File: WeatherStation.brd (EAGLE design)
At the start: 30.5 x 53.3 mm, 36 parts, among them J1 EDISON_CONNECTOR_FULLMOUNTING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, J2 EDISON_CONNECTOR_FULLHEADER, U1 MCP73831, U2 HTU21D, U3 MPL3115A2, U4 PCA9306

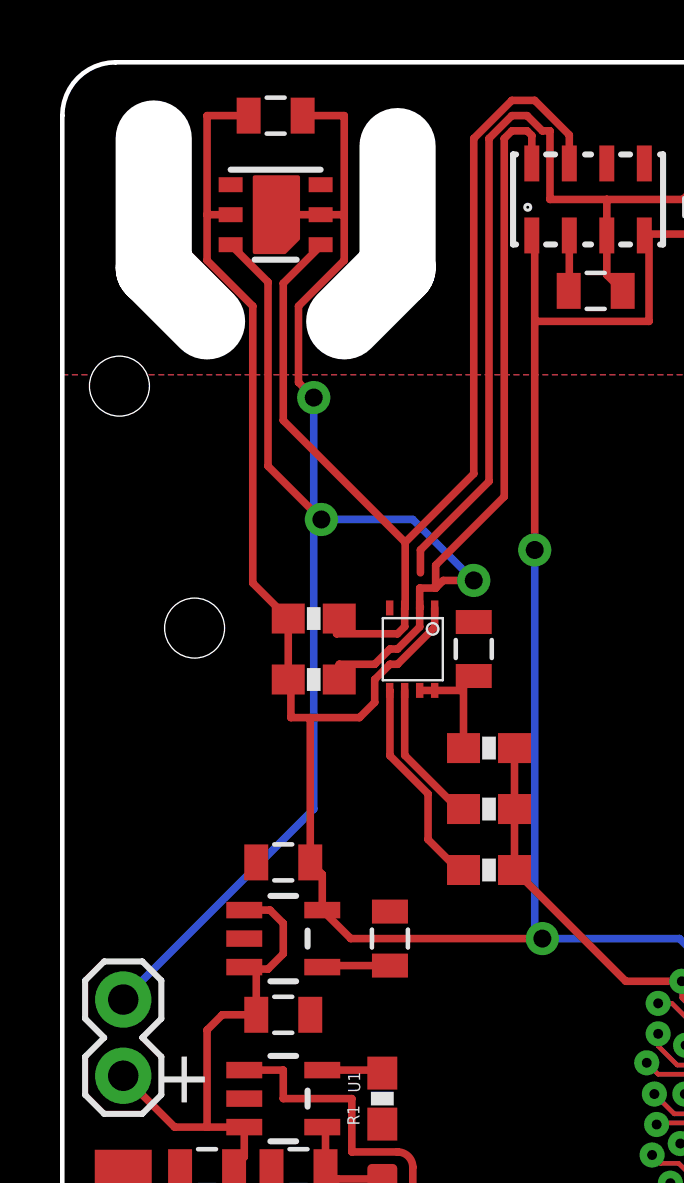
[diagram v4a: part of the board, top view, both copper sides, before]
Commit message: removed unnecessary GND trace and via
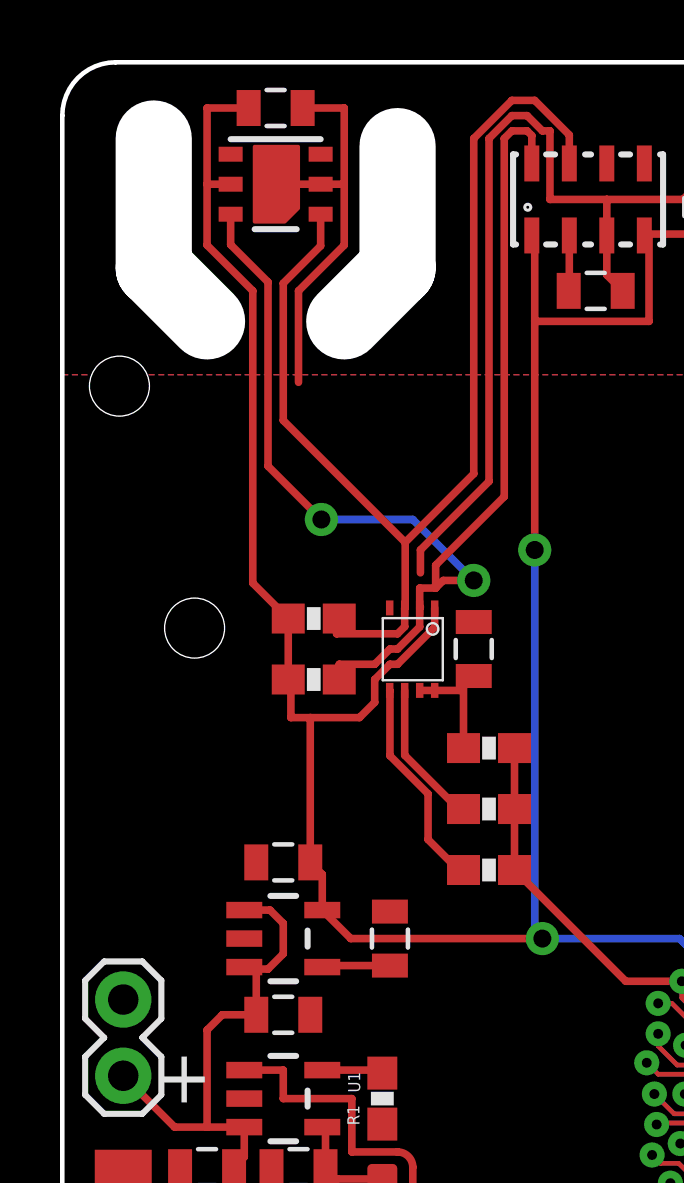
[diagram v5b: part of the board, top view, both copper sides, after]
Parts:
- moved U2 1.02 mm to (7.11, 49.3)
- moved C8 0.25 mm to (7.11, 51.8)
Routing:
- net GND: track 69.5 -> 46.4 mm, vias 3 -> 2
- net SDA: track 37.4 -> 38.4 mm
- net SCL: track 41.2 -> 42.2 mm
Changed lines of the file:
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@@
 </element>
 <element name="JP2" library="SparkFun-Connectors" package="1X02" value="M02PTH" x="2.032" y="22.098" smashed="yes" rot="R270"/>
-<element name="U2" library="SparkFun-Sensors" package="HTU21D" value="HTU21D" x="7.112" y="48.26" smashed="yes">
-<attribute name="VALUE" x="5.787" y="46.06" size="0.5" layer="27"/>
+<element name="U2" library="SparkFun-Sensors" package="HTU21D" value="HTU21D" x="7.112" y="49.276" smashed="yes">
+<attribute name="VALUE" x="5.787" y="47.076" size="0.5" layer="27"/>
 </element>
 <element name="U3" library="SparkFun-Sensors" package="LGA8" value="MPL3115A2" x="17.526" y="48.768" smashed="yes" rot="R90">
@@
 <attribute name="VALUE" x="11.684" y="26.289" size="0.4064" layer="27"/>
 </element>
-<element name="C8" library="SparkFun-Capacitors" package="0805" value="4.7µF" x="7.112" y="51.562" smashed="yes">
-<attribute name="VALUE" x="7.112" y="50.673" size="0.4064" layer="27" align="top-center"/>
+<element name="C8" library="SparkFun-Capacitors" package="0805" value="4.7µF" x="7.112" y="51.816" smashed="yes">
+<attribute name="VALUE" x="7.112" y="50.927" size="0.4064" layer="27" align="top-center"/>
 </element>
 <element name="C9" library="SparkFun-Capacitors" package="0805" value="0.1µF" x="17.78" y="45.72" smashed="yes">
@@
 <contactref element="C6" pad="2"/>
 <contactref element="C7" pad="2"/>
-<wire x1="8.012" y1="51.562" x2="9.398" y2="51.562" width="0.254" layer="1"/>
-<wire x1="9.398" y1="51.562" x2="9.398" y2="48.26" width="0.254" layer="1"/>
-<wire x1="9.398" y1="48.26" x2="9.398" y2="46.736" width="0.254" layer="1"/>
-<wire x1="9.398" y1="46.736" x2="7.874" y2="45.212" width="0.254" layer="1"/>
-<wire x1="8.612" y1="48.26" x2="9.398" y2="48.26" width="0.254" layer="1"/>
-<wire x1="8.612" y1="48.26" x2="7.112" y2="48.26" width="0.254" layer="1"/>
+<wire x1="8.612" y1="49.276" x2="7.112" y2="49.276" width="0.254" layer="1"/>
 <wire x1="18.68" y1="45.72" x2="18.151" y2="46.249" width="0.254" layer="1"/>
 <wire x1="18.151" y1="46.249" x2="18.151" y2="47.568" width="0.254" layer="1"/>
@@
 <wire x1="14.224" y1="39.37" x2="11.938" y2="37.084" width="0.254" layer="1"/>
 <wire x1="11.938" y1="37.084" x2="11.938" y2="36.322" width="0.254" layer="1"/>
-<wire x1="7.874" y1="45.212" x2="7.874" y2="42.672" width="0.254" layer="1"/>
-<wire x1="7.874" y1="42.672" x2="8.382" y2="42.164" width="0.254" layer="1"/>
-<via x="8.382" y="42.164" extent="1-16" drill="0.6" diameter="0.254"/>
-<wire x1="8.382" y1="42.164" x2="8.382" y2="28.448" width="0.254" layer="16"/>
-<wire x1="8.382" y1="28.448" x2="2.032" y2="22.098" width="0.254" layer="16"/>
 <polygon width="0.3048" layer="1">
 <vertex x="0" y="42.926"/>
@@
 <vertex x="0" y="1.778"/>
 </polygon>
+<wire x1="8.012" y1="51.816" x2="9.398" y2="51.816" width="0.254" layer="1"/>
+<wire x1="9.398" y1="51.816" x2="9.398" y2="49.276" width="0.254" layer="1"/>
+<wire x1="9.398" y1="49.276" x2="9.398" y2="47.244" width="0.254" layer="1"/>
+<wire x1="9.398" y1="47.244" x2="7.874" y2="45.72" width="0.254" layer="1"/>
+<wire x1="7.874" y1="45.72" x2="7.874" y2="42.672" width="0.254" layer="1"/>
+<wire x1="8.612" y1="49.276" x2="9.398" y2="49.276" width="0.254" layer="1"/>
+<wire x1="26.9438" y1="22.1798" x2="28.2448" y2="22.1742" width="0" layer="19" extent="1-1"/>
+<wire x1="25.96" y1="22.18" x2="26.9438" y2="22.1798" width="0" layer="19" extent="1-16"/>
+<wire x1="25.96" y1="22.1798" x2="25.96" y2="22.18" width="0" layer="19" extent="1-16"/>
+<wire x1="25.96" y1="22.98" x2="25.96" y2="22.18" width="0" layer="19" extent="16-16"/>
 <wire x1="25.96" y1="22.9798" x2="25.96" y2="22.98" width="0" layer="19" extent="1-16"/>
-<wire x1="25.96" y1="22.18" x2="25.96" y2="22.98" width="0" layer="19" extent="16-16"/>
-<wire x1="25.96" y1="22.1798" x2="25.96" y2="22.18" width="0" layer="19" extent="1-16"/>
 <wire x1="25.96" y1="21.38" x2="25.96" y2="22.18" width="0" layer="19" extent="16-16"/>
 <wire x1="25.96" y1="21.3798" x2="25.96" y2="21.38" width="0" layer="19" extent="1-16"/>
@@
 <wire x1="25.96" y1="20.18" x2="25.96" y2="20.58" width="0" layer="19" extent="16-16"/>
 <wire x1="25.96" y1="20.1798" x2="25.96" y2="20.18" width="0" layer="19" extent="1-16"/>
-<wire x1="26.9438" y1="22.1798" x2="25.96" y2="22.18" width="0" layer="19" extent="1-16"/>
 <wire x1="27.1272" y1="20.5232" x2="25.96" y2="20.58" width="0" layer="19" extent="16-16"/>
-<wire x1="28.2448" y1="22.1742" x2="26.9438" y2="22.1798" width="0" layer="19" extent="1-1"/>
-<wire x1="11.938" y1="36.322" x2="13.716" y2="34.682" width="0" layer="19" extent="1-1"/>
-<wire x1="10.914" y1="35.152" x2="11.938" y2="36.322" width="0" layer="19" extent="1-1"/>
-<wire x1="6.0659" y1="18.796" x2="6.974" y2="16.51" width="0" layer="19" extent="1-1"/>
-<wire x1="10.922" y1="25.03" x2="8.382" y2="28.448" width="0" layer="19" extent="1-16"/>
+<wire x1="10.922" y1="25.03" x2="25.96" y2="22.98" width="0" layer="19" extent="1-16"/>
+<wire x1="8.266" y1="21.59" x2="10.922" y2="25.03" width="0" layer="19" extent="1-1"/>
+<wire x1="6.0659" y1="24.13" x2="8.266" y2="21.59" width="0" layer="19" extent="1-1"/>
+<wire x1="6.466" y1="26.67" x2="6.0659" y2="24.13" width="0" layer="19" extent="1-1"/>
+<wire x1="6.0659" y1="18.796" x2="8.266" y2="21.59" width="0" layer="19" extent="1-1"/>
+<wire x1="6.974" y1="16.51" x2="6.0659" y2="18.796" width="0" layer="19" extent="1-1"/>
+<wire x1="3.926" y1="16.51" x2="6.974" y2="16.51" width="0" layer="19" extent="1-1"/>
+<wire x1="2.032" y1="16.192" x2="3.926" y2="16.51" width="0" layer="19" extent="1-1"/>
+<wire x1="10.668" y1="17.946" x2="6.974" y2="16.51" width="0" layer="19" extent="1-1"/>
+<wire x1="2.032" y1="22.098" x2="6.0659" y2="24.13" width="0" layer="19" extent="1-1"/>
+<wire x1="4.682" y1="10.892" x2="3.926" y2="16.51" width="0" layer="19" extent="1-1"/>
+<wire x1="2.032" y1="8.192" x2="4.682" y2="10.892" width="0" layer="19" extent="1-1"/>
+<wire x1="10.914" y1="35.152" x2="6.466" y2="26.67" width="0" layer="19" extent="1-1"/>
+<wire x1="11.938" y1="36.322" x2="10.914" y2="35.152" width="0" layer="19" extent="1-1"/>
+<wire x1="13.716" y1="34.682" x2="11.938" y2="36.322" width="0" layer="19" extent="1-1"/>
+<wire x1="9.398" y1="51.816" x2="14.224" y2="50.8" width="0" layer="19" extent="1-1"/>
 </signal>
 <signal name="VSYS">
@@
 <contactref element="C10" pad="A"/>
 <contactref element="C7" pad="1"/>
-<wire x1="6.212" y1="51.562" x2="4.826" y2="51.562" width="0.254" layer="1"/>
-<wire x1="4.826" y1="51.562" x2="4.826" y2="48.26" width="0.254" layer="1"/>
-<wire x1="4.826" y1="48.26" x2="4.826" y2="46.736" width="0.254" layer="1"/>
-<wire x1="4.826" y1="46.736" x2="6.35" y2="45.212" width="0.254" layer="1"/>
-<wire x1="5.612" y1="48.26" x2="4.826" y2="48.26" width="0.254" layer="1"/>
+<wire x1="4.826" y1="51.816" x2="4.826" y2="49.276" width="0.254" layer="1"/>
 <wire x1="19.401" y1="47.568" x2="19.447" y2="47.614" width="0.254" layer="1"/>
 <wire x1="19.447" y1="47.614" x2="21.336" y2="47.614" width="0.254" layer="1"/>
@@
 <wire x1="7.532" y1="34.798" x2="7.532" y2="32.766" width="0.254" layer="1"/>
 <wire x1="7.532" y1="34.798" x2="6.35" y2="35.98" width="0.254" layer="1"/>
-<wire x1="6.35" y1="35.98" x2="6.35" y2="45.212" width="0.254" layer="1"/>
+<wire x1="6.35" y1="35.98" x2="6.35" y2="45.72" width="0.254" layer="1"/>
 <wire x1="15.748" y1="44.704" x2="15.748" y2="37.084" width="0.254" layer="1"/>
 <via x="15.748" y="37.084" extent="1-16" drill="0.6" diameter="0.254"/>
 <wire x1="15.748" y1="37.084" x2="15.748" y2="24.384" width="0.254" layer="16"/>
 <wire x1="15.748" y1="24.384" x2="16.002" y2="24.13" width="0.254" layer="16"/>
+<wire x1="5.612" y1="49.276" x2="4.826" y2="49.276" width="0.254" layer="1"/>
+<wire x1="6.35" y1="45.72" x2="4.826" y2="47.244" width="0.254" layer="1"/>
+<wire x1="4.826" y1="47.244" x2="4.826" y2="49.276" width="0.254" layer="1"/>
+<wire x1="4.826" y1="51.816" x2="6.212" y2="51.816" width="0.254" layer="1"/>
 </signal>
 <signal name="GP183_PWM3">
@@
 <wire x1="11.43" y1="37.338" x2="11.43" y2="35.168" width="0.254" layer="1"/>
 <wire x1="11.43" y1="35.168" x2="11.414" y2="35.152" width="0.254" layer="1"/>
-<wire x1="8.612" y1="47.26" x2="8.612" y2="47.22" width="0.254" layer="1"/>
-<wire x1="8.612" y1="47.22" x2="7.366" y2="45.974" width="0.254" layer="1"/>
 <wire x1="7.366" y1="45.974" x2="7.366" y2="41.402" width="0.254" layer="1"/>
 <wire x1="7.366" y1="41.402" x2="11.43" y2="37.338" width="0.254" layer="1"/>
+<wire x1="8.612" y1="48.276" x2="8.612" y2="47.22" width="0.254" layer="1"/>
+<wire x1="8.612" y1="47.22" x2="7.366" y2="45.974" width="0.254" layer="1"/>
 </signal>
 <signal name="SCL">
 <contactref element="U2" pad="SCK"/>
 <contactref element="U4" pad="2"/>
-<wire x1="5.612" y1="47.26" x2="6.858" y2="46.014" width="0.254" layer="1"/>
 <contactref element="U3" pad="8"/>
 <wire x1="15.651" y1="49.968" x2="15.651" y2="50.897" width="0.254" layer="1"/>
@@
 <wire x1="13.716" y1="36.068" x2="12.7" y2="36.068" width="0.254" layer="1"/>
 <wire x1="12.7" y1="36.068" x2="12.446" y2="35.814" width="0.254" layer="1"/>
+<wire x1="6.858" y1="46.014" x2="5.612" y2="47.26" width="0.254" layer="1"/>
+<wire x1="5.612" y1="47.26" x2="5.612" y2="48.276" width="0.254" layer="1"/>
 </signal>
 <signal name="N$3">

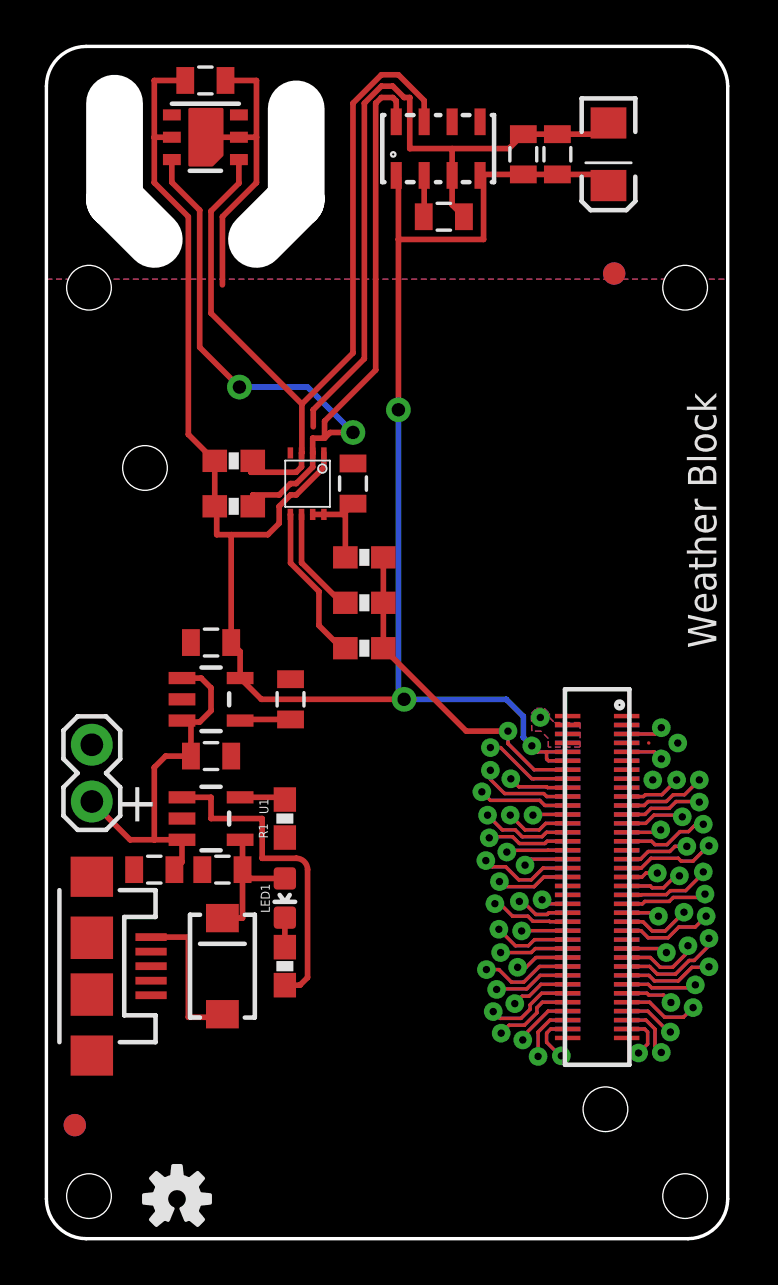
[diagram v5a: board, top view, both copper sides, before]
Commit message: moved bottom GND plane out of antenna keep out
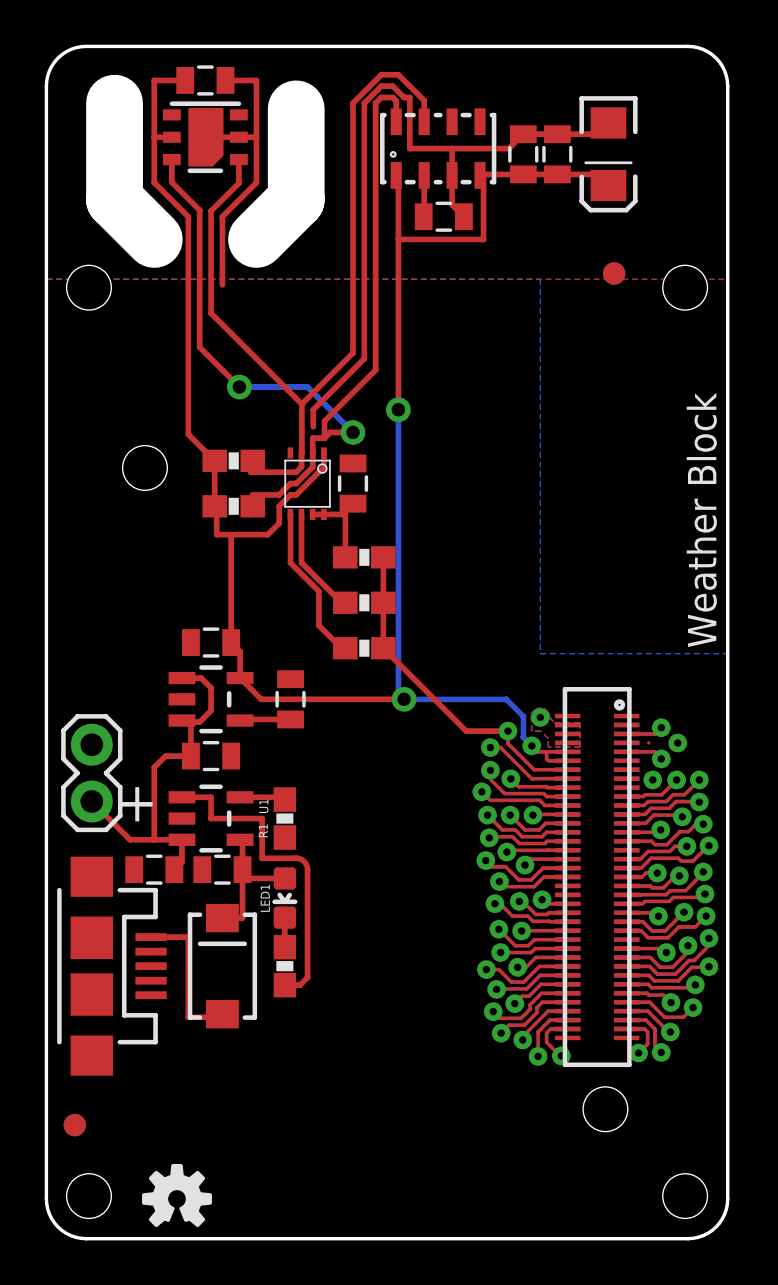
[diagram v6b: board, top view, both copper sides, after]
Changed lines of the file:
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@@
 <polygon width="0.3048" layer="16">
 <vertex x="0" y="42.926"/>
-<vertex x="30.48" y="42.926"/>
+<vertex x="22.098" y="42.926"/>
+<vertex x="22.098" y="26.162"/>
+<vertex x="30.48" y="26.162"/>
 <vertex x="30.48" y="1.778" curve="-90"/>
 <vertex x="28.702" y="0"/>
@@
 <wire x1="7.874" y1="45.72" x2="7.874" y2="42.672" width="0.254" layer="1"/>
 <wire x1="8.612" y1="49.276" x2="9.398" y2="49.276" width="0.254" layer="1"/>
-<wire x1="26.9438" y1="22.1798" x2="28.2448" y2="22.1742" width="0" layer="19" extent="1-1"/>
-<wire x1="25.96" y1="22.18" x2="26.9438" y2="22.1798" width="0" layer="19" extent="1-16"/>
+<wire x1="25.96" y1="22.9798" x2="25.96" y2="22.98" width="0" layer="19" extent="1-16"/>
+<wire x1="25.96" y1="22.18" x2="25.96" y2="22.98" width="0" layer="19" extent="16-16"/>
 <wire x1="25.96" y1="22.1798" x2="25.96" y2="22.18" width="0" layer="19" extent="1-16"/>
-<wire x1="25.96" y1="22.98" x2="25.96" y2="22.18" width="0" layer="19" extent="16-16"/>
-<wire x1="25.96" y1="22.9798" x2="25.96" y2="22.98" width="0" layer="19" extent="1-16"/>
 <wire x1="25.96" y1="21.38" x2="25.96" y2="22.18" width="0" layer="19" extent="16-16"/>
 <wire x1="25.96" y1="21.3798" x2="25.96" y2="21.38" width="0" layer="19" extent="1-16"/>
@@
 <wire x1="25.96" y1="20.18" x2="25.96" y2="20.58" width="0" layer="19" extent="16-16"/>
 <wire x1="25.96" y1="20.1798" x2="25.96" y2="20.18" width="0" layer="19" extent="1-16"/>
+<wire x1="26.9438" y1="22.1798" x2="25.96" y2="22.18" width="0" layer="19" extent="1-16"/>
 <wire x1="27.1272" y1="20.5232" x2="25.96" y2="20.58" width="0" layer="19" extent="16-16"/>
-<wire x1="10.922" y1="25.03" x2="25.96" y2="22.98" width="0" layer="19" extent="1-16"/>
-<wire x1="8.266" y1="21.59" x2="10.922" y2="25.03" width="0" layer="19" extent="1-1"/>
-<wire x1="6.0659" y1="24.13" x2="8.266" y2="21.59" width="0" layer="19" extent="1-1"/>
-<wire x1="6.466" y1="26.67" x2="6.0659" y2="24.13" width="0" layer="19" extent="1-1"/>
-<wire x1="6.0659" y1="18.796" x2="8.266" y2="21.59" width="0" layer="19" extent="1-1"/>
-<wire x1="6.974" y1="16.51" x2="6.0659" y2="18.796" width="0" layer="19" extent="1-1"/>
-<wire x1="3.926" y1="16.51" x2="6.974" y2="16.51" width="0" layer="19" extent="1-1"/>
-<wire x1="2.032" y1="16.192" x2="3.926" y2="16.51" width="0" layer="19" extent="1-1"/>
-<wire x1="10.668" y1="17.946" x2="6.974" y2="16.51" width="0" layer="19" extent="1-1"/>
-<wire x1="2.032" y1="22.098" x2="6.0659" y2="24.13" width="0" layer="19" extent="1-1"/>
-<wire x1="4.682" y1="10.892" x2="3.926" y2="16.51" width="0" layer="19" extent="1-1"/>
-<wire x1="2.032" y1="8.192" x2="4.682" y2="10.892" width="0" layer="19" extent="1-1"/>
-<wire x1="10.914" y1="35.152" x2="6.466" y2="26.67" width="0" layer="19" extent="1-1"/>
-<wire x1="11.938" y1="36.322" x2="10.914" y2="35.152" width="0" layer="19" extent="1-1"/>
-<wire x1="13.716" y1="34.682" x2="11.938" y2="36.322" width="0" layer="19" extent="1-1"/>
+<wire x1="28.2448" y1="22.1742" x2="26.9438" y2="22.1798" width="0" layer="19" extent="1-1"/>
+<wire x1="11.938" y1="36.322" x2="13.716" y2="34.682" width="0" layer="19" extent="1-1"/>
+<wire x1="10.914" y1="35.152" x2="11.938" y2="36.322" width="0" layer="19" extent="1-1"/>
+<wire x1="6.0659" y1="18.796" x2="6.974" y2="16.51" width="0" layer="19" extent="1-1"/>
+<wire x1="10.922" y1="25.03" x2="8.266" y2="21.59" width="0" layer="19" extent="1-1"/>
 <wire x1="9.398" y1="51.816" x2="14.224" y2="50.8" width="0" layer="19" extent="1-1"/>
 </signal>
